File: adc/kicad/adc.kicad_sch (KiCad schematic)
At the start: 106 parts, among them J1 Conn_01x02_Pin, J2 Conn_01x02_Pin, J3 Conn_01x02_Pin, J5 Conn_01x07_Pin, J6 pcie_98, U1 ADS1261BIRHBT, U2 ESD5344D-TP, U3 TPS7A2050PDBVR, U4 TPS7A2025PDBVRr, U6 TPS65135, U7 ADP7182AUJZ-5.0, U8 ADP7182AUJZ-2.5, U9 XC6206P332MR

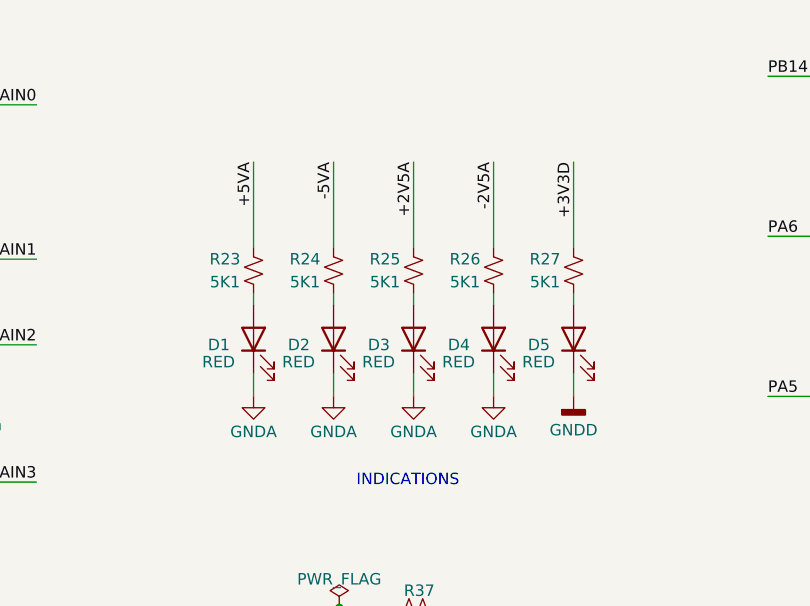
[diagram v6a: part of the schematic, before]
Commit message: Tweaked the ADC layout.
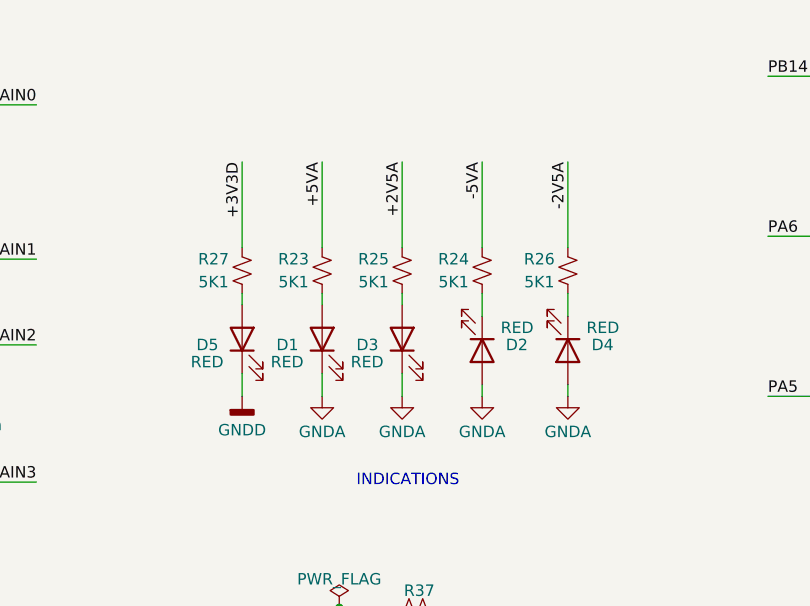
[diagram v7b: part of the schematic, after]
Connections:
- net GNDA: now also D2.2 (A), D4.2 (A); no longer D2.1 (K), D4.1 (K)
- net at R26.2: now also D4.1 (K); no longer D4.2 (A)
- net at R24.2: now also D2.1 (K); no longer D2.2 (A)
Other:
- moved on the sheet: D1, D2, D3, D4, D5, R23, R24, R25, R26, R27

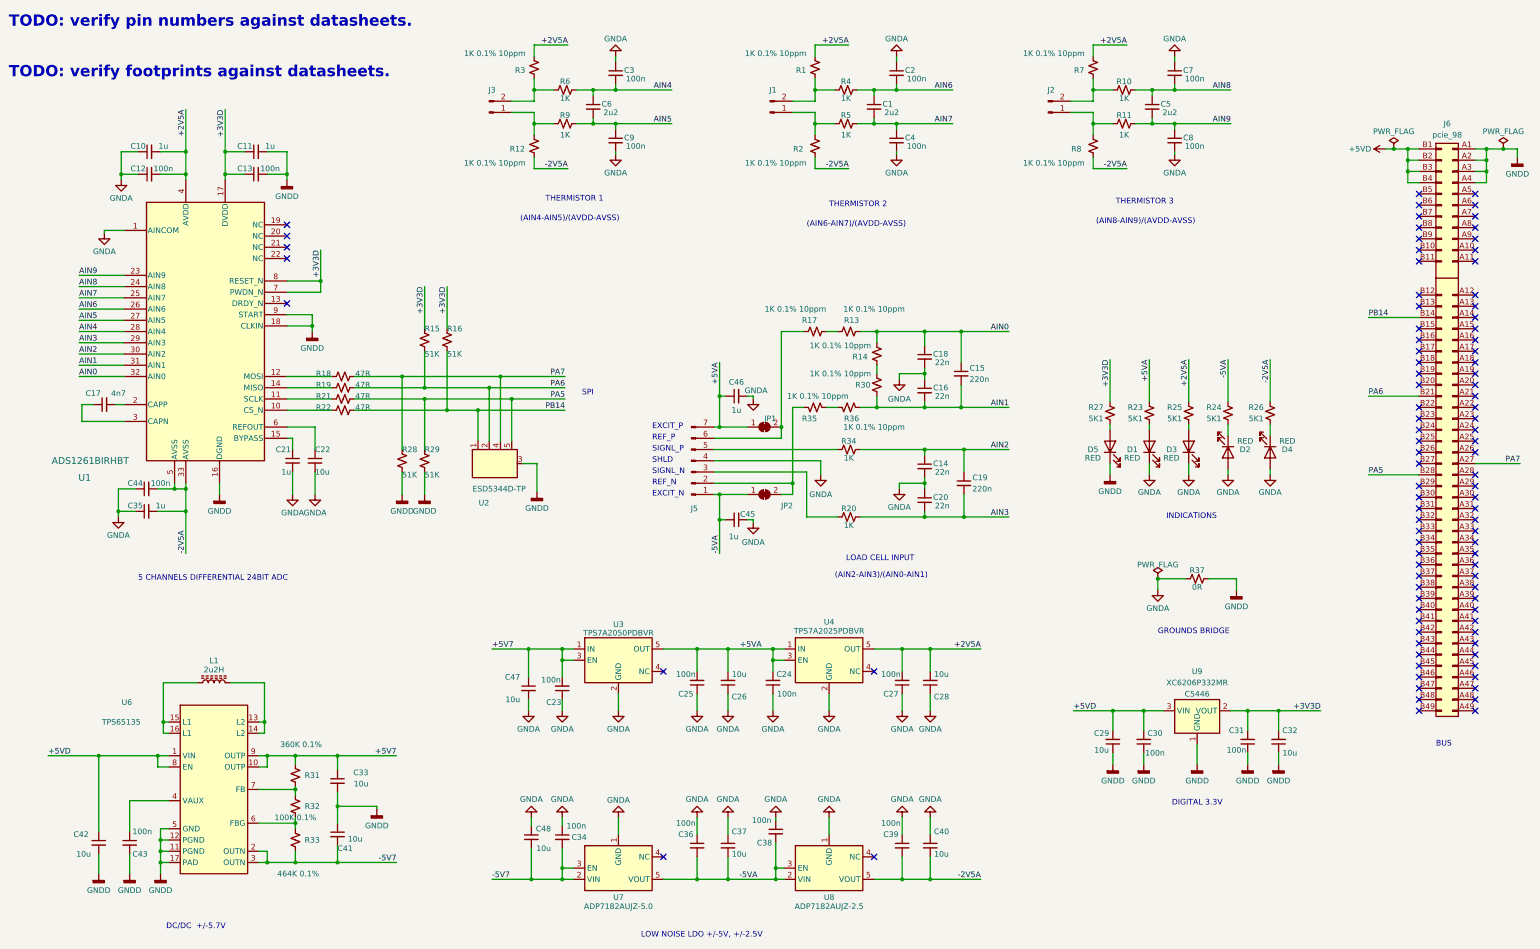
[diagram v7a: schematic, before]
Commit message: More ADC layout touchups.
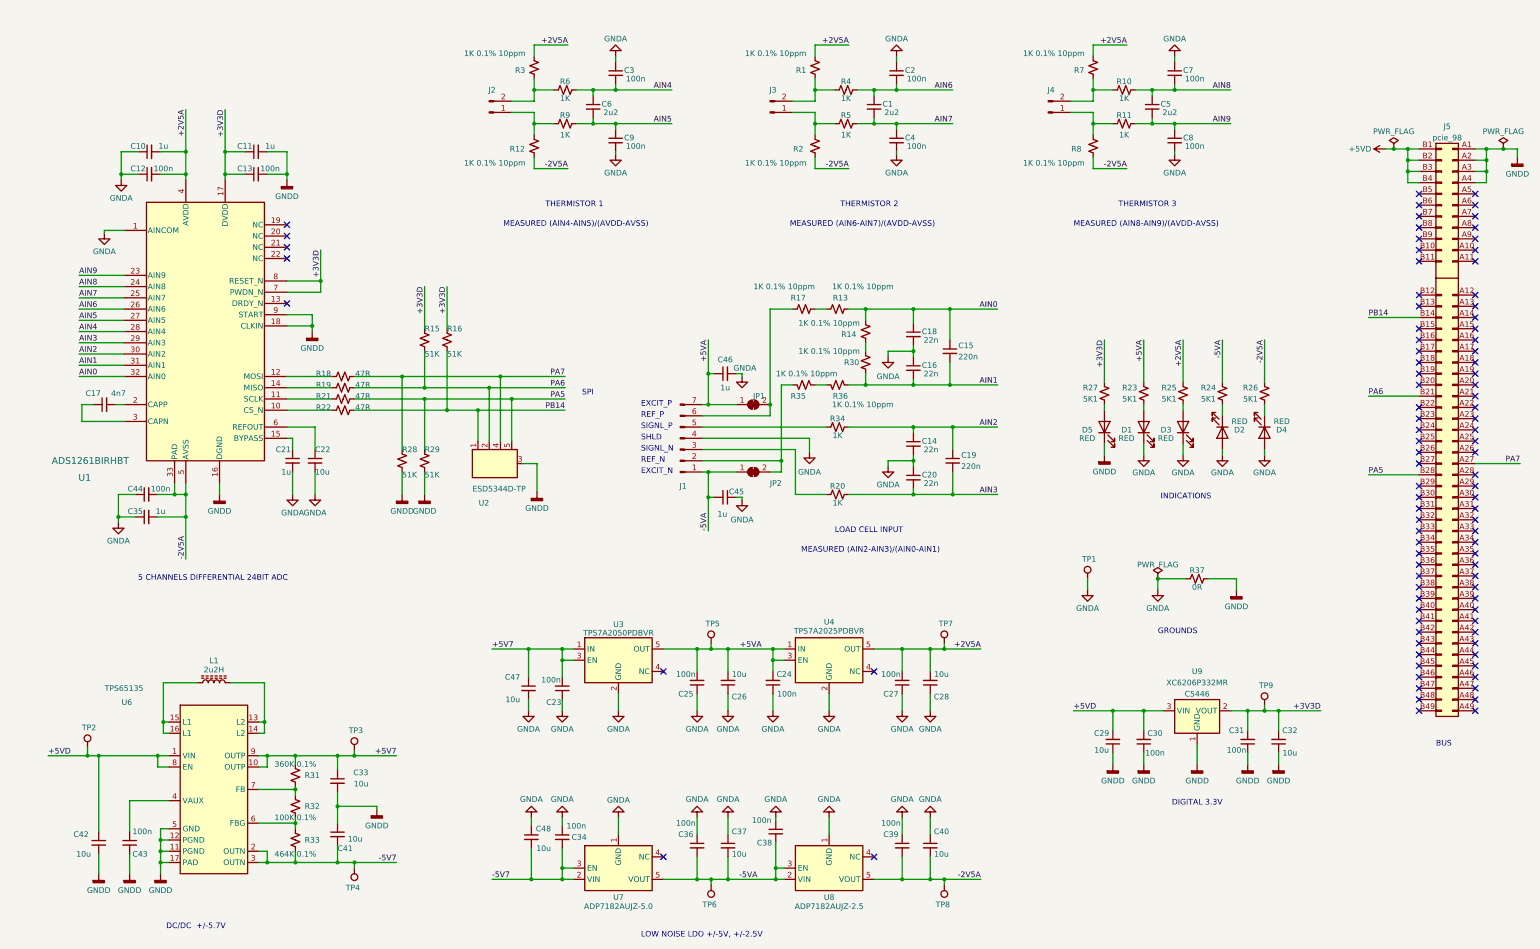
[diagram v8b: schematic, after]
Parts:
- added TP1, TP2, TP3, TP4, TP5, TP6, TP7, TP8, TP9: TestPoint, common:Test_Pad, symbol Connector:TestPoint
- renumbered J5 to J1, J3 to J2, J1 to J3, J2 to J4, J6 to J5
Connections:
- net +2V5A: now also TP7.1
- net +3V3D: now also TP9.1
- net +5V7: now also TP3.1
- net +5VA: now also TP5.1
- net +5VD: now also TP2.1
- net -2V5A: now also TP8.1
- net -5V7: now also TP4.1
- net -5VA: now also TP6.1
- net GNDA: now also TP1.1
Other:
- note added: "GROUNDS"
- note added: "MEASURED (AIN2-AIN3)/(AIN0-AIN1)"
- note added: "MEASURED (AIN4-AIN5)/(AVDD-AVSS)"
- note added: "MEASURED (AIN6-AIN7)/(AVDD-AVSS)"
- note added: "MEASURED (AIN8-AIN9)/(AVDD-AVSS)"
- note removed: "(AIN2-AIN3)/(AIN0-AIN1)"
- note removed: "(AIN4-AIN5)/(AVDD-AVSS)"
- note removed: "(AIN6-AIN7)/(AVDD-AVSS)"
- note removed: "(AIN8-AIN9)/(AVDD-AVSS)"
- note removed: "GROUNDS BRIDGE"
- note removed: "TODO: verify footprints against datasheets."
- note removed: "TODO: verify pin numbers against datasheets."
- moved on the sheet: C14, C15, C16, C18, C19, C20, C35, C44, C45, C46, D1, D2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
